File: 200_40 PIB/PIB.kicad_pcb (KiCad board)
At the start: 2 copper layers, 80 x 49 mm, 192 parts, among them J1 M80-5100442, J10 53261-0671, J11 53261-0271, J12 M80-5100842, J13 53261-0271, J15 53261-0571, J2 53261-0471, J3 G125-MS12605M2P, J4 53261-0671, J5 53261-1371, J6 MMCX, J7 BNC, J8 SWD/DEBUG, J9 53261-0671, Q1 Si7489DP, Q10 IRF7832, Q11 IRF7832, Q2 Si7489DP, Q9 IRF7832, SW1 6mm tact, U1 LT3065EDDPBF, U10 LT8580EDD, U11 OP37, U12 MAX823TEUK_T, U13 74LVC1G18DBV, U14 74HC08PW, U15 74HC08PW, U16 74LVC2G157DCU, U17 74LVC1G18DBV, U2 MIC4424YM, U3 MIC4424YM, U4 STM32G431RBTx, U5 ADM1270ACPZ, U6 LM1117MP-3.3, U7 ADM1270ACPZ, U8 74LVC1GU04DRL, U9 74LVC2G126DCU, Y1 ECS-80-18-4XDN

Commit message: prelim layout for pib mainboard v1. TODO review
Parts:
- removed C25: 100nF, Capacitor_SMD:C_0402_1005Metric
- added C61: 100nF, Capacitor_SMD:C_0402_1005Metric, B.Cu at (224.4, 111.6)
- added R87: 10K, Resistor_SMD:R_0402_1005Metric, B.Cu at (224.4, 110.6)
- C1, C20, C45, C47, C48, C55, C56, C6, D1, R26, R27, R28, R29, R30, R31, R32, R33, R82, R83, R84, R85, R86, U1, U10, U12, U13, U16, U17, U8, U9: moved to B.Cu
- C10, C11, C22, C31, C43, C44, C46, C49, C53: footprint Capacitor_SMD:C_0603_1608Metric -> Capacitor_SMD:C_0402_1005Metric; moved to B.Cu
- C23, C24, C26, C27, C29, C30, C34, C35, C36, C40, C41, C42, C5, C50, C51, C52, C54: footprint Capacitor_SMD:C_0603_1608Metric -> Capacitor_SMD:C_0402_1005Metric
- H1, H2, H3, H4: value M3 -> M2.5; footprint MountingHole:MountingHole_3.2mm_M3_DIN965_Pad -> MountingHole:MountingHole_2.7mm_M2.5_DIN965_Pad
- J10, J4, J9: value 53261-0671 -> 53398-0671; footprint Connector_Molex:Molex_PicoBlade_53261-0671_1x06-1MP_P1.25mm_Horizontal -> Connector_Molex:Molex_PicoBlade_53398-0671_1x06-1MP_P1.25mm_Vertical
- J11, J13: value 53261-0271 -> 53398-0271; footprint Connector_Molex:Molex_PicoBlade_53261-0271_1x02-1MP_P1.25mm_Horizontal -> Connector_Molex:Molex_PicoBlade_53398-0271_1x02-1MP_P1.25mm_Vertical
- J15: value 53261-0571 -> 53398-0571; footprint Connector_Molex:Molex_PicoBlade_53261-0571_1x05-1MP_P1.25mm_Horizontal -> Connector_Molex:Molex_PicoBlade_53398-0571_1x05-1MP_P1.25mm_Vertical
- J2: value 53261-0471 -> 53398-0471; footprint Connector_Molex:Molex_PicoBlade_53261-0471_1x04-1MP_P1.25mm_Horizontal -> Connector_Molex:Molex_PicoBlade_53398-0471_1x04-1MP_P1.25mm_Vertical
- J5: value 53261-1371 -> 53398-1371; footprint Connector_Molex:Molex_PicoBlade_53261-1371_1x13-1MP_P1.25mm_Horizontal -> Connector_Molex:Molex_PicoBlade_53398-1371_1x13-1MP_P1.25mm_Vertical
- J6: footprint Connector_Coaxial:MMCX_Molex_73415-0961_Horizontal_1.6mm-PCB -> Connector_Coaxial:MMCX_Molex_73415-1471_Vertical
- J7: value BNC -> MMCX; footprint Connector_Coaxial:BNC_Amphenol_B6252HB-NPP3G-50_Horizontal -> Connector_Coaxial:MMCX_Molex_73415-1471_Vertical
- J8: footprint Connector_PinSocket_2.54mm:PinSocket_2x03_P2.54mm_Vertical -> Connector_PinHeader_2.54mm:PinHeader_2x03_P2.54mm_Vertical_SMD
- R1, R17, R18, R19, R2, R3, R36, R37, R43, R44, R47, R5, R6, R66, R67, R68, R69, R7, R75, R76, R77, R78, R8: footprint Resistor_SMD:R_0603_1608Metric -> Resistor_SMD:R_0402_1005Metric; moved to B.Cu
- R10, R11, R12, R13, R14, R15, R16, R20, R21, R34, R38, R39, R4, R40, R41, R42, R48, R49, R50, R51, R52, R53, R54, R55, R56, R57, R58, R59, R60, R61, R62, R63, R64, R70, R71, R72, R73, R74, R9: footprint Resistor_SMD:R_0603_1608Metric -> Resistor_SMD:R_0402_1005Metric
- Y1: value ECS-80-18-4XDN -> ABM3B-8.000MHZ-10-D1G-T; footprint Crystal:Crystal_HC49-U_Vertical -> Crystal:Crystal_SMD_Abracon_ABM3B-4Pin_5.0x3.2mm
- moved H4 160.2 mm to (257.0, 137.5)
- moved H2 159.1 mm to (257.0, 94.5)
- moved C5 156.7 mm to (259.9, 104.3), turned to 90 degrees
- moved C9 155.3 mm to (258.8, 104.0), turned to 90 degrees
- moved U16 153.3 mm to (233.6, 100.8), turned to -90 degrees
- moved C60 149.9 mm to (257.8, 134.0)
- moved C55 149.1 mm to (248.8, 96.4), turned to 180 degrees
- moved R26 146.8 mm to (246.7, 97.2), turned to 90 degrees
- moved R27 146.5 mm to (245.5, 97.2), turned to 90 degrees
- moved R13 146.2 mm to (257.5, 107.3), turned to 180 degrees
- moved R28 146.1 mm to (244.2, 97.2), turned to 90 degrees
- moved U17 145.9 mm to (242.4, 100.9), turned to -90 degrees
- moved R82 145.9 mm to (243.0, 97.2), turned to 90 degrees
- moved C58 144.6 mm to (256.3, 98.0), turned to 180 degrees
- moved R15 144.2 mm to (259.4, 107.3)
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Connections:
- C22 pad 1: 12V -> +12V
- C40 pad 2: Net-(D1-K) -> GND
- C6 pad 1: 12V -> +12V
- D1 pad 1: Net-(D1-K) -> GND
- J12 pad 8: GND -> /ADC_NTC_DCHG
- J5 pad 7: 5V -> +5V
- R18 pad 1: 12V -> +12V
- R29 pad 1: /IGNITER -> /IGNITER_PULSE_GATED
- U1 pad 10: 12V -> +12V
- U1 pad 9: 12V -> +12V
- U10 pad 9: Net-(D1-K) -> GND
- U15 pad 2: /VALVE2_H -> /VALVE3_H
- U15 pad 3: /VALVE2_H_GATED -> /VALVE3_H_GATED
- U15 pad 5: /VALVE2_L -> /VALVE3_L
- U15 pad 6: /VALVE2_L_GATED -> /VALVE3_L_GATED
- U2 pad 5: Net-(J4-Pin_2) -> Net-(J4-Pin_1)
- U2 pad 7: Net-(J4-Pin_1) -> Net-(J4-Pin_2)
- U3 pad 5: Net-(J4-Pin_4) -> Net-(J4-Pin_3)
- U3 pad 7: Net-(J4-Pin_3) -> Net-(J4-Pin_4)
- U4 pad 45: /DISCHARGE_RST -> unconnected-(U4-PA11-Pad45)
- Y1 pad 2: Net-(U4-PF0) -> GND
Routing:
- net +5V: track 0.00 -> 161.0 mm, vias 0 -> 6
- net -5V: track 0.00 -> 132.0 mm, vias 0 -> 5
- net /ARM/~{SAFE}: track 0.00 -> 87.8 mm, vias 0 -> 4
- net /ADC_NTC_DCHG: track 0.00 -> 58.6 mm, vias 0 -> 2
- net /ADC_TANK_NTC_2: track 0.00 -> 55.7 mm, vias 0 -> 3
- net /EXT_SPI_~{CS}: track 0.00 -> 54.6 mm, vias 0 -> 2
- net /EXT_SPI_SCK: track 0.00 -> 52.9 mm, vias 0 -> 2
- net /ADC_TANK_NTC_1: track 0.00 -> 51.3 mm, vias 0 -> 2
- net /EXT_SPI_MISO: track 0.00 -> 51.1 mm, vias 0 -> 2
- net /DRDY: track 0.00 -> 50.9 mm, vias 0 -> 3
- net /EXT_SPI_MOSI: track 0.00 -> 50.4 mm, vias 0 -> 2
- net Net-(U12-~{MR}): track 0.00 -> 48.3 mm, vias 0 -> 1
- net /IGNITER_PGOOD: track 0.00 -> 47.8 mm, vias 0 -> 2
- net /DISCHARGE_PGOOD: track 0.00 -> 47.5 mm, vias 0 -> 4
- net /INT_I2C_SDA: track 0.00 -> 46.6 mm, vias 0 -> 4
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- added copper zone on B.Cu, net +12V
- added copper zone on In2.Cu, net +3.3V
- added copper zone on F.Cu, net +5V
- added copper zone on F.Cu, net -5V
- added copper zone on B.Cu, net BAT_HOT
- added copper zone on F.Cu, net BAT_HOT
- added copper zone on B.Cu, net GND
- added copper zone on F.Cu, net GND
- added copper zone on In1.Cu, net GND
- added copper zone on F.Cu, net Net-(D1-A)
- added copper zone on F.Cu, net Net-(J2-Pin_1)
- added copper zone on F.Cu, net Net-(J2-Pin_4)
- added copper zone on F.Cu, net Net-(U10-SW)
- added copper zone on B.Cu, net Net-(U5-SENSE-)
- added copper zone on B.Cu, net Net-(U7-SENSE-)
- added copper zone on B.Cu, net VBAT_DCHG
- added copper zone on B.Cu, net VBAT_IGN
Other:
- copper layers 2 -> 4
- board text added: "DIO | RX CLK | TX RST | GND"
- board text added: "DISCHARGE SUPPLY"
- board text added: "FLOW SENSOR"
- board text added: "FRIT DPT"
- board text added: "GSE VALVE OVERRIDE"
- board text added: "IGNITER SUPPLY"
- board text added: "PIB Mainboard Rev 1.0 Alan Hsu"
- board text added: "ROGOWSKI"
- board text added: "TANK DPT"
- board text added: "TANK HTRS"
- board text added: "TANK NTC"
- board text added: "TO CDH"
- board text added: "VALVES"
- board text added: "V_DCHG"

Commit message: fix DRC warnings, check DRC rules against JLC spec, replace all connector symbols with proper MP symbols (MP to ground), fix ground stitching
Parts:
- Y1: footprint Crystal:Crystal_SMD_Abracon_ABM3B-4Pin_5.0x3.2mm -> 0_PAY_Footprint_Library:Crystal_SMD_Abracon_ABM3B-4Pin_5.0x3.2mm
- moved C10 0.30 mm to (220.7, 126.7)
- moved C11 0.30 mm to (222.6, 127.7)
- moved R2 0.30 mm to (220.7, 127.7)
- moved R75 0.20 mm to (206.7, 111.2)
- moved R45 0.20 mm to (243.8, 132.7)
- moved R46 0.20 mm to (246.8, 132.7)
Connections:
- J10 pad MP: (no net) -> GND
- J11 pad MP: (no net) -> GND
- J13 pad MP: (no net) -> GND
- J15 pad MP: (no net) -> GND
- J2 pad MP: (no net) -> GND
- J3 pad MP: (no net) -> GND
- J4 pad MP: (no net) -> GND
- J5 pad MP: (no net) -> GND
- J9 pad MP: (no net) -> GND
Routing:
- net +3.3V: track 21.2 -> 22.2 mm
- net Net-(J3-Pin_21): track 45.7 -> 45.2 mm
- net GND: vias 72 -> 89

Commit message: add TVS diodes
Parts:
- added C25: 1uF, Capacitor_SMD:C_0603_1608Metric, B.Cu at (212.1, 93.7)
- added C62: 1uF, Capacitor_SMD:C_0603_1608Metric, B.Cu at (217.9, 136.7)
- added C63: 1uF, Capacitor_SMD:C_0603_1608Metric, B.Cu at (210.6, 93.7)
- added C64: 1uF, Capacitor_SMD:C_0603_1608Metric, B.Cu at (195.6, 131.6)
- added C65: 1uF, Capacitor_SMD:C_0603_1608Metric, B.Cu at (195.6, 133.4)
- added C66: 1uF, Capacitor_SMD:C_0603_1608Metric, B.Cu at (209.4, 133.4)
- added C67: 1uF, Capacitor_SMD:C_0603_1608Metric, B.Cu at (205.9, 95.4)
- added C68: 10uF, Capacitor_SMD:C_0805_2012Metric, B.Cu at (232.2, 137.5)
- added D10: SMF14A, Diode_SMD:D_SMF, F.Cu at (250.9, 132.7)
- added D12: PESD5V0S1UL, Diode_SMD:D_SOD-882, F.Cu at (210.2, 131.4)
- added D13: SMF18A, Diode_SMD:D_SMF, B.Cu at (214.6, 137.1)
- added D14: SMF18A, Diode_SMD:D_SMF, B.Cu at (220.2, 137.1)
- added D15: PESD3V3U1UL, Diode_SMD:D_SOD-882, B.Cu at (217.5, 95.0)
- added D16: PESD3V3U1UL, Diode_SMD:D_SOD-882, B.Cu at (220.1, 95.0)
- added D17: ESDA5V3SC5, Package_TO_SOT_SMD:SOT-23-5, B.Cu at (256.8, 115.4)
- added D18: PESD5V0S1UL, Diode_SMD:D_SOD-882, F.Cu at (246.4, 112.3)
- added D19: PESD3V3U1UL, Diode_SMD:D_SOD-882, B.Cu at (228.2, 95.2)
- added D2: PESD3V3U1UL, Diode_SMD:D_SOD-882, B.Cu at (193.6, 115.9)
- added D20: PESD3V3U1UL, Diode_SMD:D_SOD-882, B.Cu at (242.7, 95.2)
- added D21: PESD3V3U1UL, Diode_SMD:D_SOD-882, B.Cu at (197.4, 116.1)
- added D22: PESD3V3U1UL, Diode_SMD:D_SOD-882, B.Cu at (195.3, 112.9)
- added D23: PESD3V3U1UL, Diode_SMD:D_SOD-882, B.Cu at (196.6, 111.7)
- added D24: PESD3V3U1UL, Diode_SMD:D_SOD-882, B.Cu at (216.2, 95.0)
- added D25: PESD3V3U1UL, Diode_SMD:D_SOD-882, B.Cu at (214.9, 95.0)
- added D26: PESD3V3U1UL, Diode_SMD:D_SOD-882, B.Cu at (213.6, 95.0)
- added D27: PESD3V3U1UL, Diode_SMD:D_SOD-882, B.Cu at (218.8, 95.0)
- added D28: PESD3V3U1UL, Diode_SMD:D_SOD-882, B.Cu at (229.4, 95.2)
- added D29: PESD3V3U1UL, Diode_SMD:D_SOD-882, B.Cu at (230.7, 95.2)
- added D3: SMF18A, Diode_SMD:D_SMF, F.Cu at (196.4, 126.1)
- added D30: PESD3V3U1UL, Diode_SMD:D_SOD-882, B.Cu at (232.0, 95.2)
- added D31: PESD3V3U1UL, Diode_SMD:D_SOD-882, B.Cu at (244.0, 95.2)
- added D32: PESD3V3U1UL, Diode_SMD:D_SOD-882, B.Cu at (245.3, 95.2)
- added D33: PESD3V3U1UL, Diode_SMD:D_SOD-882, B.Cu at (246.6, 95.2)
- added D34: PESD3V3U1UL, Diode_SMD:D_SOD-882, B.Cu at (259.8, 106.1)
- added D35: PESD3V3U1UL, Diode_SMD:D_SOD-882, B.Cu at (259.8, 107.4)
- added D4: PESD3V3U1UL, Diode_SMD:D_SOD-882, B.Cu at (195.7, 114.4)
- added D5: PESD3V3U1UL, Diode_SMD:D_SOD-882, B.Cu at (242.4, 133.7)
- added D6: SP0502BAJT, Package_TO_SOT_SMD:SOT-323_SC-70, B.Cu at (190.3, 112.1)
- added D7: PESD5V0S1UL, Diode_SMD:D_SOD-882, F.Cu at (259.8, 128.0)
- added D8: PESD5V0S1UL, Diode_SMD:D_SOD-882, F.Cu at (261.2, 115.0)
- added D9: PESD5V0S1UL, Diode_SMD:D_SOD-882, B.Cu at (194.1, 105.3)
- SW1: value 6mm tact -> B3F-1000
- moved R36 3.55 mm to (224.4, 113.8), turned to 0 degrees
- moved R37 3.50 mm to (225.0, 117.3), turned to -90 degrees
- moved R32 1.00 mm to (225.1, 114.8), turned to 0 degrees
- moved R33 1.00 mm to (225.1, 115.8), turned to 0 degrees
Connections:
- J3 pad 20: Net-(J3-Pin_20) -> /EXT_I2C_SCL
- J3 pad 21: Net-(J3-Pin_21) -> /EXT_I2C_SDA
- R32 pad 1: /EXT_I2C_SCL -> /EXT_I2C_SDA
- R32 pad 2: Net-(J3-Pin_20) -> Net-(U4-PA8)
- R33 pad 1: /EXT_I2C_SDA -> /EXT_I2C_SCL
- R33 pad 2: Net-(J3-Pin_21) -> Net-(U4-PA9)
- R36 pad 1: /EXT_I2C_SCL -> /EXT_I2C_SDA
- R37 pad 1: /EXT_I2C_SDA -> /EXT_I2C_SCL
- U4 pad 42: /EXT_I2C_SDA -> Net-(U4-PA8)
- U4 pad 43: /EXT_I2C_SCL -> Net-(U4-PA9)
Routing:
- net /EXT_I2C_SCL: track 2.48 -> 48.3 mm
- net /EXT_I2C_SDA: track 2.74 -> 48.2 mm
- net Net-(J3-Pin_21): track 45.2 -> 0.00 mm, vias 1 -> 0
- net Net-(J3-Pin_20): track 45.1 -> 0.00 mm, vias 1 -> 0
- net /SWDIO: track 3.88 -> 11.1 mm, vias 0 -> 1
- net /SWDCLK: track 3.86 -> 10.7 mm, vias 0 -> 1
- net -5V: track 132.2 -> 138.5 mm, vias 5 -> 6
- net /ADC_TANK_NTC_1: track 51.3 -> 55.8 mm
- net /ADC_V_IGN_SUPPLY: track 30.7 -> 34.7 mm, vias 2 -> 3
- net /ADC_I_IGN_PK: track 30.2 -> 33.5 mm, vias 2 -> 3
- net GND: track 12.4 -> 15.6 mm, vias 89 -> 113
- net /ADC_V_IGN_PK: track 21.9 -> 25.0 mm, vias 0 -> 1
- net +5V: track 161.0 -> 164.0 mm
- net +12V: track 29.6 -> 31.5 mm
- net 12V_GSE: track 12.0 -> 13.7 mm
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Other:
- board text added: "GSE"
- board text removed: "GSE VALVE OVERRIDE"

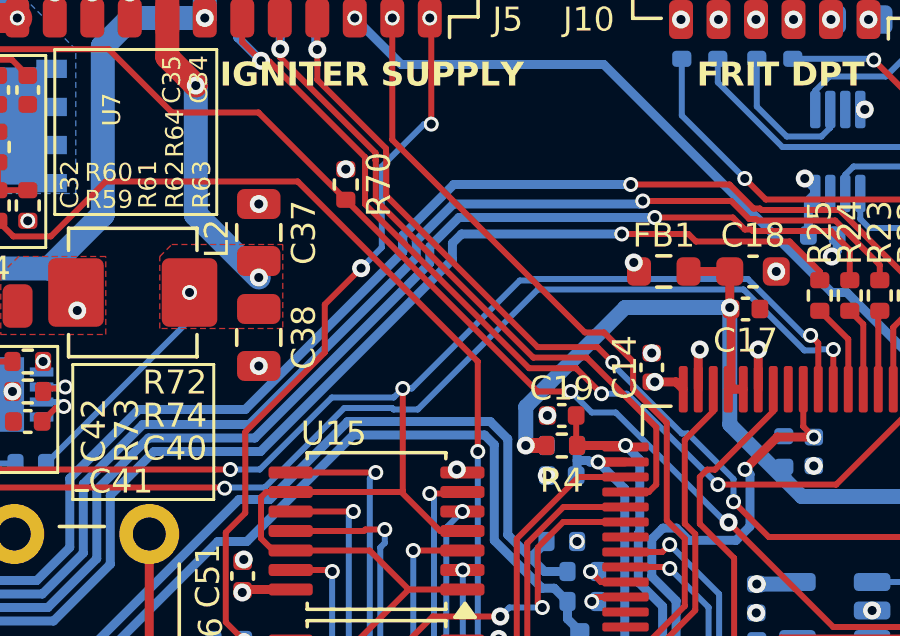
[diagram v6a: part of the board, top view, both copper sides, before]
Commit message: clean up schematic
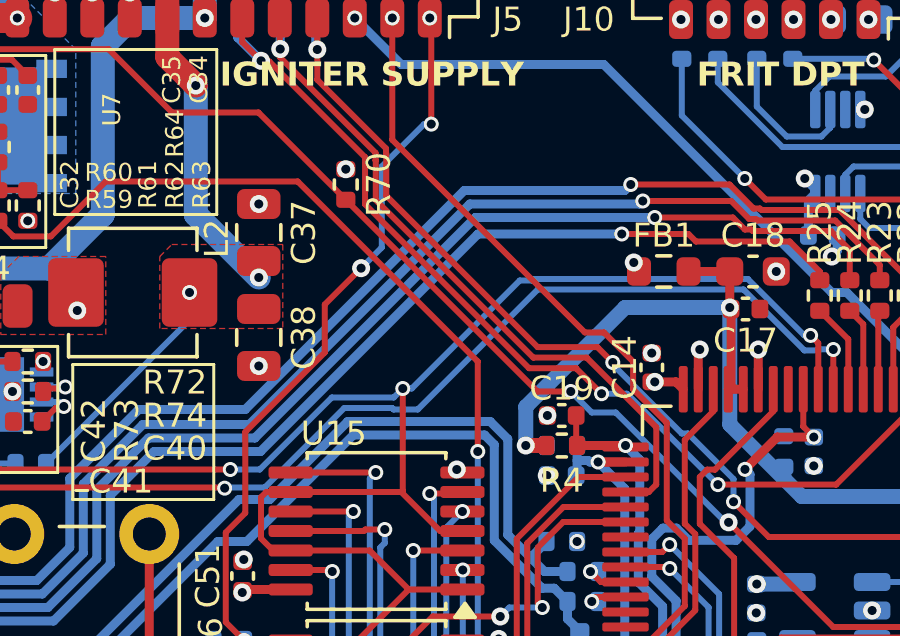
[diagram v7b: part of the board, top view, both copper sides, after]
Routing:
- net /EXT_SPI_~{CS}: track 54.6 -> 53.9 mm
